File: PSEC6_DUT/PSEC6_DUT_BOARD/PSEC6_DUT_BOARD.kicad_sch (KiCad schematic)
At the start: 1 part

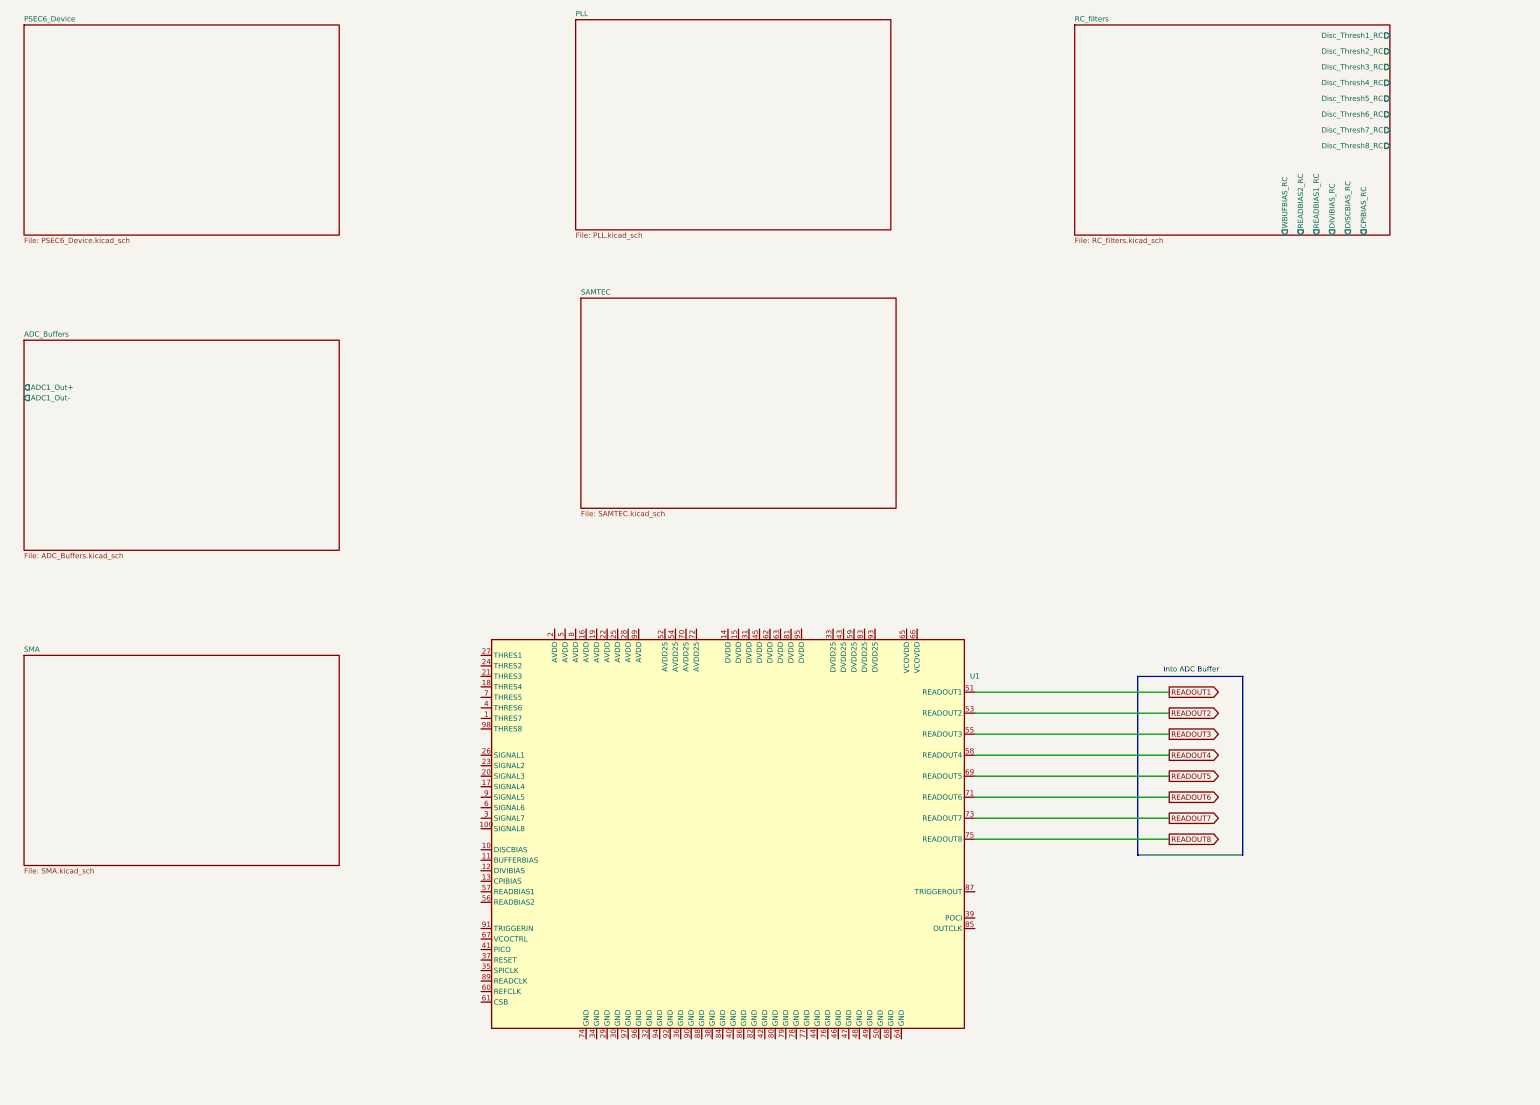
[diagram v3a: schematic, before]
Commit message: DUT Board Schematic Done besides SAMTEC
The DUT Board is now done and fully documented besides the placement of the signals on the SAMTEC connector between the two boards, as the position of each connection will be determined during layout.
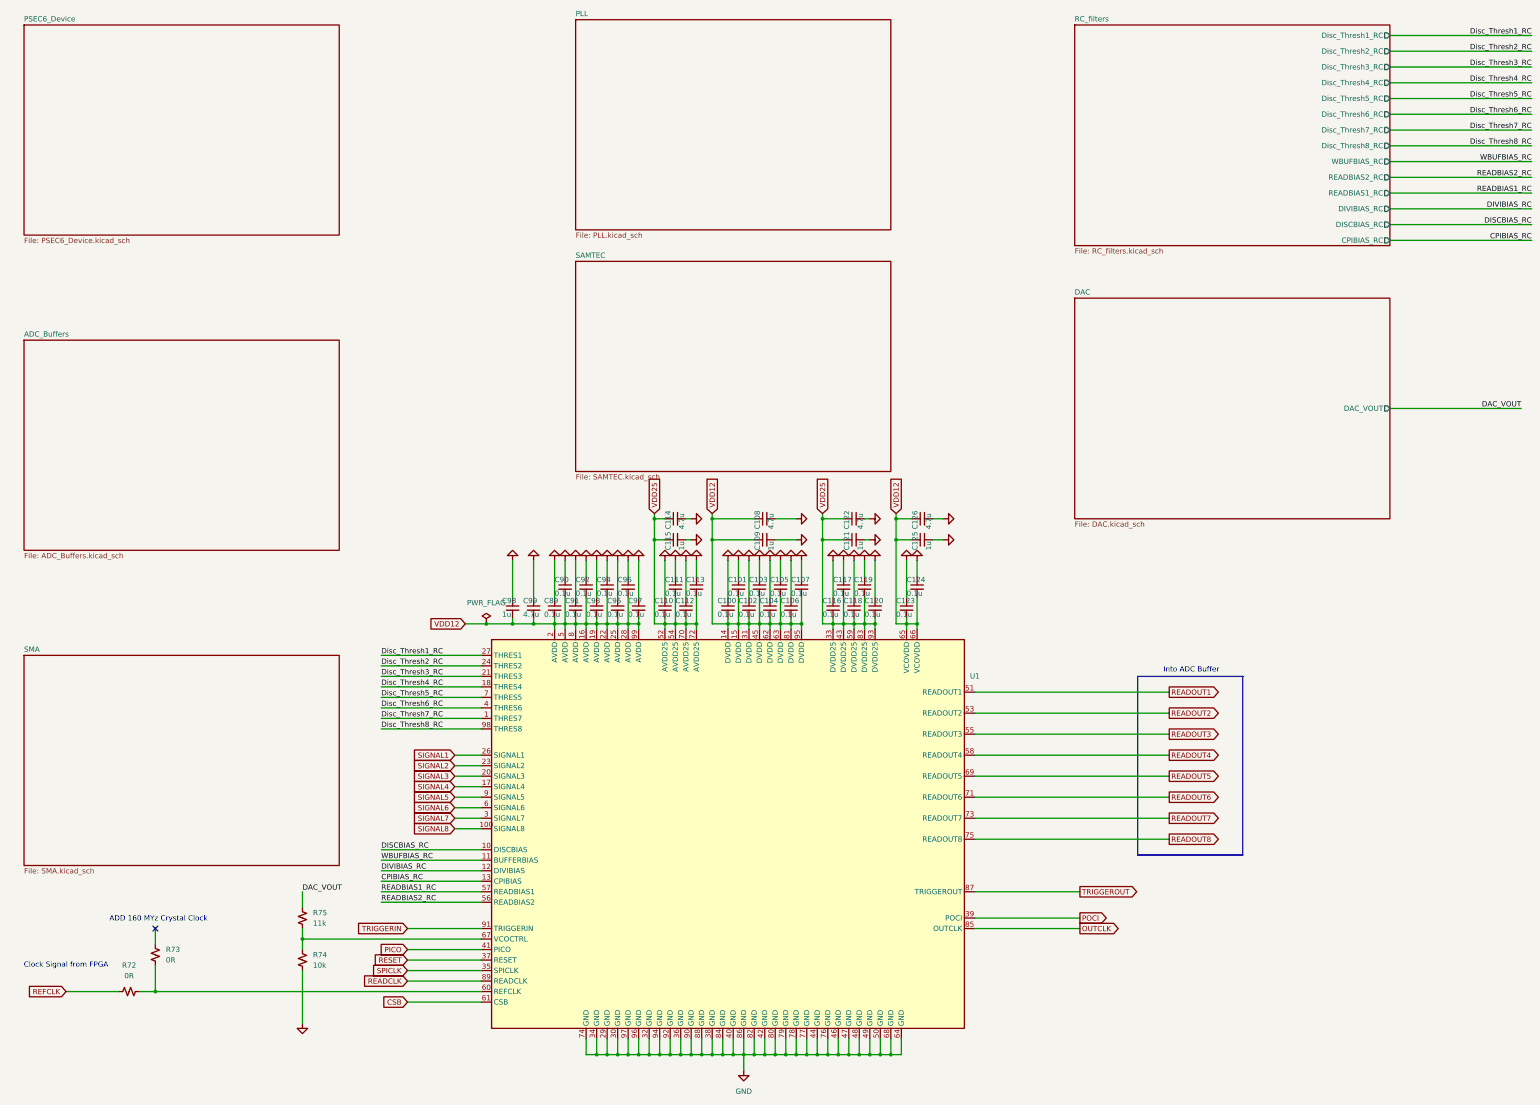
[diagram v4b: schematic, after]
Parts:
- added C100, C101, C102, C103, C104, C105, C106, C107, C110, C111, C112, C113, C116, C117, C118, C119, C120, C123, C124, C89, C90, C91, C92, C93, C94, C95, C96, C97: 0.1u, Capacitor_SMD:C_0603_1608Metric, symbol Device:C_Small
- added C108, C114, C122, C126, C99: 4.7u, Capacitor_SMD:C_0603_1608Metric, symbol Device:C_Small
- added C109, C115, C121, C125, C98: 1u, Capacitor_SMD:C_0603_1608Metric, symbol Device:C_Small
- added R72, R73: 0R, Resistor_SMD:R_0603_1608Metric, symbol Device:R_Small_US
- added R74: 10k, Resistor_SMD:R_0603_1608Metric, symbol Device:R_Small_US
- added R75: 11k, Resistor_SMD:R_0603_1608Metric, symbol Device:R_Small_US
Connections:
- net Disc_Thresh7_RC: now reaches U1.1 (THRES7)
- net DISCBIAS_RC: now reaches U1.10 (DISCBIAS)
- net SIGNAL8: now reaches U1.100 (SIGNAL8)
- net WBUFBIAS_RC: now reaches U1.11 (BUFFERBIAS)
- net DIVIBIAS_RC: now reaches U1.12 (DIVIBIAS)
- net CPIBIAS_RC: now reaches U1.13 (CPIBIAS)
- net VDD12: now reaches U1.14 (DVDD)
- net VDD12: now also U1.15 (DVDD), U1.16 (AVDD), U1.19 (AVDD), U1.2 (AVDD), U1.22 (AVDD), U1.25 (AVDD), U1.28 (AVDD), U1.31 (DVDD), U1.45 (DVDD), U1.5 (AVDD), U1.62 (DVDD), U1.63 (DVDD), U1.65 (VCOVDD), U1.66 (VCOVDD), U1.8 (AVDD), U1.81 (DVDD), U1.95 (DVDD), U1.99 (AVDD), C100.2, C101.2, C102.2, C103.2, C104.2, C105.2, C106.2, C107.2, C108.1, C109.1, C123.2, C124.2, C125.1, C126.1, C89.2, C90.2, C91.2, C92.2, C93.2, C94.2, C95.2, C96.2, C97.2, C98.2, C99.2
- net SIGNAL4: now reaches U1.17 (SIGNAL4)
- net Disc_Thresh4_RC: now reaches U1.18 (THRES4)
- net SIGNAL3: now reaches U1.20 (SIGNAL3)
- net Disc_Thresh3_RC: now reaches U1.21 (THRES3)
- net SIGNAL2: now reaches U1.23 (SIGNAL2)
- net Disc_Thresh2_RC: now reaches U1.24 (THRES2)
- net SIGNAL1: now reaches U1.26 (SIGNAL1)
- net Disc_Thresh1_RC: now reaches U1.27 (THRES1)
- net GND: now reaches U1.29 (GND)
- net GND: now also U1.30 (GND), U1.32 (GND), U1.34 (GND), U1.36 (GND), U1.38 (GND), U1.40 (GND), U1.42 (GND), U1.44 (GND), U1.46 (GND), U1.47 (GND), U1.48 (GND), U1.49 (GND), U1.50 (GND), U1.64 (GND), U1.68 (GND), U1.74 (GND), U1.76 (GND), U1.77 (GND), U1.78 (GND), U1.79 (GND), U1.80 (GND), U1.82 (GND), U1.84 (GND), U1.86 (GND), U1.88 (GND), U1.90 (GND), U1.92 (GND), U1.94 (GND), U1.96 (GND), U1.97 (GND), C100.1, C101.1, C102.1, C103.1, C104.1, C105.1, C106.1, C107.1, C108.2, C109.2, C110.1, C111.1, C112.1, C113.1, C114.2, C115.2, C116.1, C117.1, C118.1, C119.1, C120.1, C121.2, C122.2, C123.1, C124.1, C125.2, C126.2, C89.1, C90.1, C91.1, C92.1, C93.1, C94.1, C95.1, C96.1, C97.1, C98.1, C99.1, R74.1
- net SIGNAL7: now reaches U1.3 (SIGNAL7)
- net VDD25: now reaches U1.33 (DVDD25)
- net VDD25: now also U1.43 (DVDD25), U1.52 (AVDD25), U1.54 (AVDD25), U1.59 (DVDD25), U1.70 (AVDD25), U1.72 (AVDD25), U1.83 (DVDD25), U1.93 (DVDD25), C110.2, C111.2, C112.2, C113.2, C114.1, C115.1, C116.2, C117.2, C118.2, C119.2, C120.2, C121.1, C122.1
- net SPICLK: now reaches U1.35 (SPICLK)
- net RESET: now reaches U1.37 (RESET)
- net POCI: now reaches U1.39 (POCI)
- net Disc_Thresh6_RC: now reaches U1.4 (THRES6)
- net PICO: now reaches U1.41 (PICO)
- net READBIAS2_RC: now reaches U1.56 (READBIAS2)
- net READBIAS1_RC: now reaches U1.57 (READBIAS1)
- net SIGNAL6: now reaches U1.6 (SIGNAL6)
- net at U1.60 (REFCLK): now also R72.2, R73.1
- net CSB: now reaches U1.61 (CSB)
- net at U1.67 (VCOCTRL): now also R74.2, R75.1
- net Disc_Thresh5_RC: now reaches U1.7 (THRES5)
- net OUTCLK: now reaches U1.85 (OUTCLK)
- net TRIGGEROUT: now reaches U1.87 (TRIGGEROUT)
- net READCLK: now reaches U1.89 (READCLK)
- net SIGNAL5: now reaches U1.9 (SIGNAL5)
- net TRIGGERIN: now reaches U1.91 (TRIGGERIN)
- net Disc_Thresh8_RC: now reaches U1.98 (THRES8)
- new net DAC_VOUT: R75.2
- new net REFCLK: R72.1
- no-connect marks 0 -> 1
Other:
- added sheet DAC (DAC.kicad_sch)
- sheet ADC_Buffers ports: added none; removed ADC1_Out+, ADC1_Out-
- note added: "ADD 160 MYz Crystal Clock"
- note added: "Clock Signal from FPGA"
